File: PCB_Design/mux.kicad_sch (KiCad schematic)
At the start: 8 parts, among them U26 SN74HC595, U27 SN74HC595, U28 ADG1406BRUZ-REEL7, U29 ADG1406BRUZ-REEL7, U30 ADG1406BRUZ-REEL7, U31 ADG1406BRUZ-REEL7

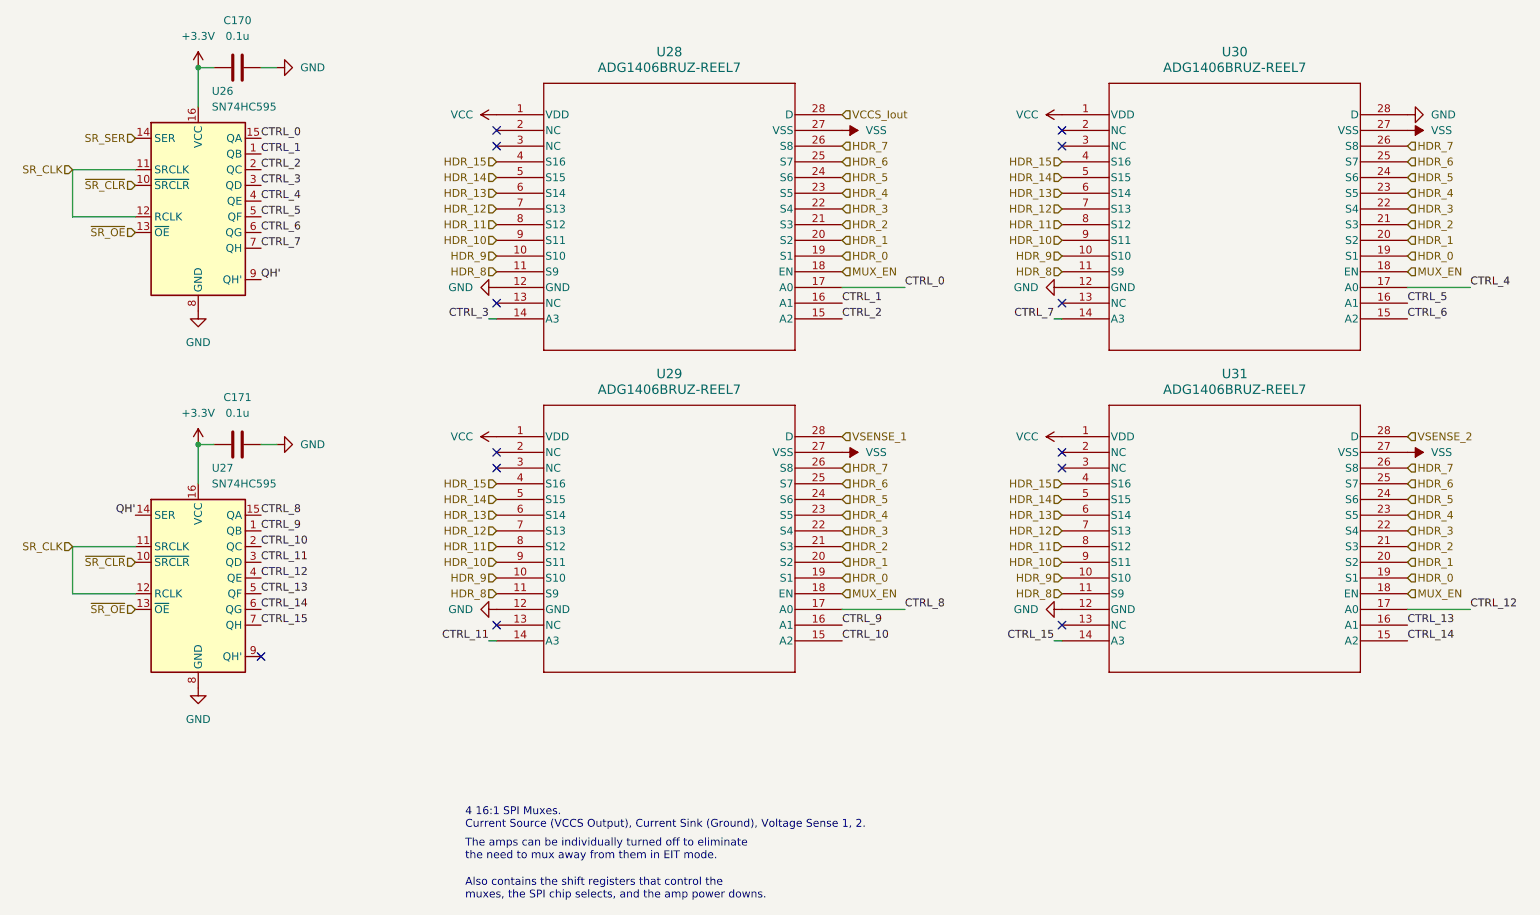
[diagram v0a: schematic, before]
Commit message: KiCAD file update, completed PCB
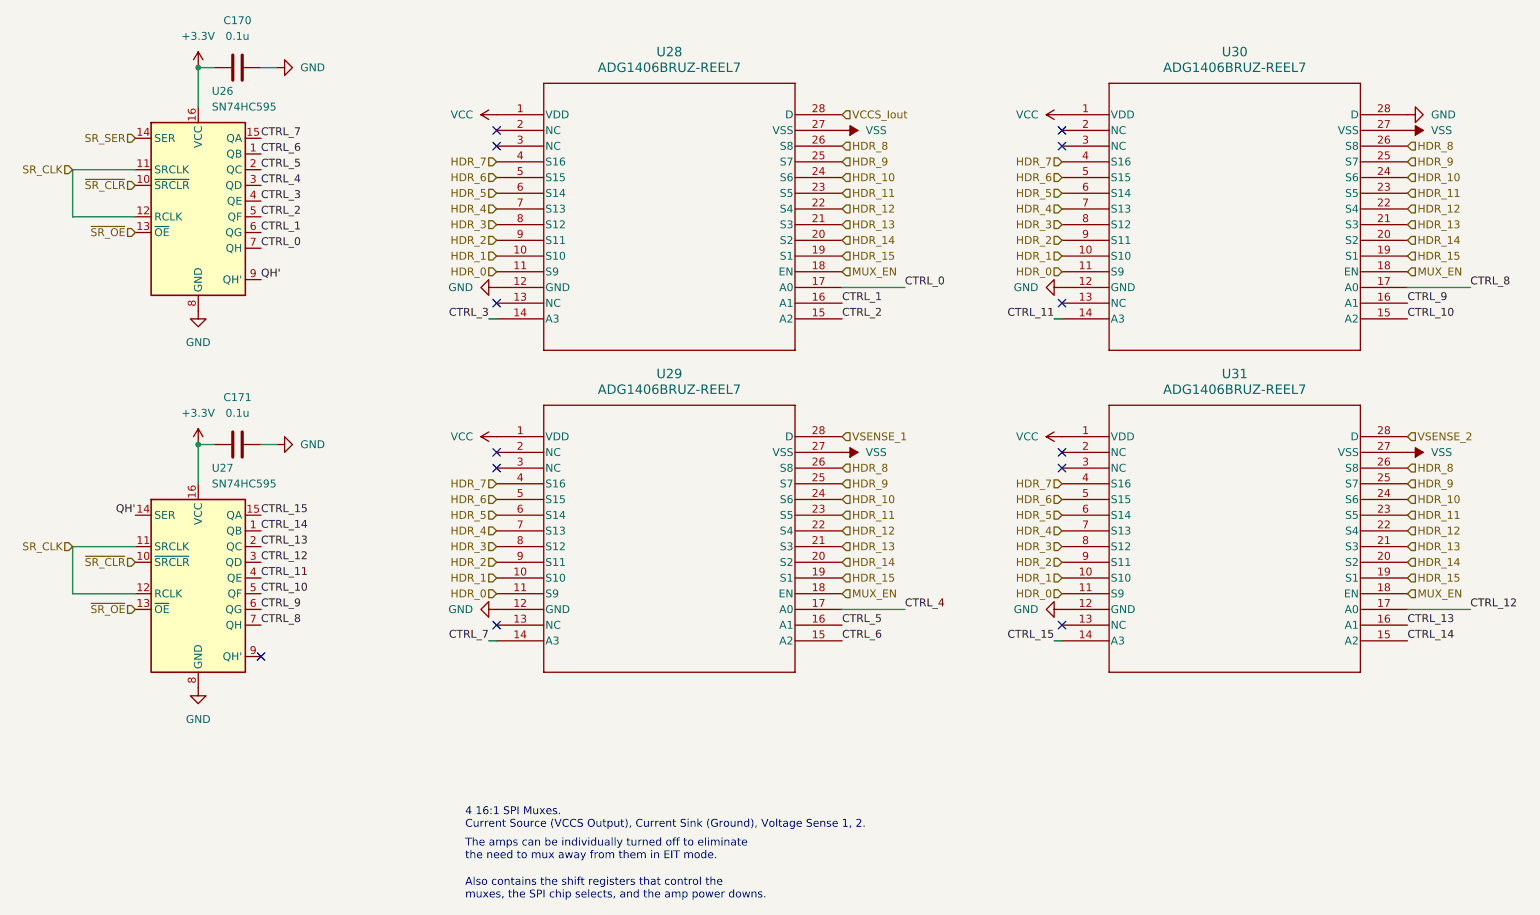
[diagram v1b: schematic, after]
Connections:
- net CTRL_0: now also U26.7 (QH); no longer U26.15 (QA)
- net CTRL_1: now also U26.6 (QG); no longer U26.1 (QB)
- net CTRL_10: now also U27.5 (QF), U30.15 (A2); no longer U27.2 (QC), U29.15 (A2)
- net CTRL_11: now also U27.4 (QE), U30.14 (A3); no longer U27.3 (QD), U29.14 (A3)
- net CTRL_12: now also U27.3 (QD); no longer U27.4 (QE)
- net CTRL_13: now also U27.2 (QC); no longer U27.5 (QF)
- net CTRL_14: now also U27.1 (QB); no longer U27.6 (QG)
- net CTRL_15: now also U27.15 (QA); no longer U27.7 (QH)
- net CTRL_2: now also U26.5 (QF); no longer U26.2 (QC)
- net CTRL_3: now also U26.4 (QE); no longer U26.3 (QD)
- net CTRL_4: now also U26.3 (QD), U29.17 (A0); no longer U26.4 (QE), U30.17 (A0)
- net CTRL_5: now also U26.2 (QC), U29.16 (A1); no longer U26.5 (QF), U30.16 (A1)
- net CTRL_6: now also U26.1 (QB), U29.15 (A2); no longer U26.6 (QG), U30.15 (A2)
- net CTRL_7: now also U26.15 (QA), U29.14 (A3); no longer U26.7 (QH), U30.14 (A3)
- net CTRL_8: now also U27.7 (QH), U30.17 (A0); no longer U27.15 (QA), U29.17 (A0)
- net CTRL_9: now also U27.6 (QG), U30.16 (A1); no longer U27.1 (QB), U29.16 (A1)
- net HDR_0: now also U28.11 (S9), U29.11 (S9), U30.11 (S9), U31.11 (S9); no longer U28.19 (S1), U29.19 (S1), U30.19 (S1), U31.19 (S1)
- net HDR_1: now also U28.10 (S10), U29.10 (S10), U30.10 (S10), U31.10 (S10); no longer U28.20 (S2), U29.20 (S2), U30.20 (S2), U31.20 (S2)
- net HDR_10: now also U28.24 (S6), U29.24 (S6), U30.24 (S6), U31.24 (S6); no longer U28.9 (S11), U29.9 (S11), U30.9 (S11), U31.9 (S11)
- net HDR_11: now also U28.23 (S5), U29.23 (S5), U30.23 (S5), U31.23 (S5); no longer U28.8 (S12), U29.8 (S12), U30.8 (S12), U31.8 (S12)
- net HDR_12: now also U28.22 (S4), U29.22 (S4), U30.22 (S4), U31.22 (S4); no longer U28.7 (S13), U29.7 (S13), U30.7 (S13), U31.7 (S13)
- net HDR_13: now also U28.21 (S3), U29.21 (S3), U30.21 (S3), U31.21 (S3); no longer U28.6 (S14), U29.6 (S14), U30.6 (S14), U31.6 (S14)
- net HDR_14: now also U28.20 (S2), U29.20 (S2), U30.20 (S2), U31.20 (S2); no longer U28.5 (S15), U29.5 (S15), U30.5 (S15), U31.5 (S15)
- net HDR_15: now also U28.19 (S1), U29.19 (S1), U30.19 (S1), U31.19 (S1); no longer U28.4 (S16), U29.4 (S16), U30.4 (S16), U31.4 (S16)
- net HDR_2: now also U28.9 (S11), U29.9 (S11), U30.9 (S11), U31.9 (S11); no longer U28.21 (S3), U29.21 (S3), U30.21 (S3), U31.21 (S3)
- net HDR_3: now also U28.8 (S12), U29.8 (S12), U30.8 (S12), U31.8 (S12); no longer U28.22 (S4), U29.22 (S4), U30.22 (S4), U31.22 (S4)
- net HDR_4: now also U28.7 (S13), U29.7 (S13), U30.7 (S13), U31.7 (S13); no longer U28.23 (S5), U29.23 (S5), U30.23 (S5), U31.23 (S5)
- net HDR_5: now also U28.6 (S14), U29.6 (S14), U30.6 (S14), U31.6 (S14); no longer U28.24 (S6), U29.24 (S6), U30.24 (S6), U31.24 (S6)
- net HDR_6: now also U28.5 (S15), U29.5 (S15), U30.5 (S15), U31.5 (S15); no longer U28.25 (S7), U29.25 (S7), U30.25 (S7), U31.25 (S7)
- net HDR_7: now also U28.4 (S16), U29.4 (S16), U30.4 (S16), U31.4 (S16); no longer U28.26 (S8), U29.26 (S8), U30.26 (S8), U31.26 (S8)
- net HDR_8: now also U28.26 (S8), U29.26 (S8), U30.26 (S8), U31.26 (S8); no longer U28.11 (S9), U29.11 (S9), U30.11 (S9), U31.11 (S9)
- net HDR_9: now also U28.25 (S7), U29.25 (S7), U30.25 (S7), U31.25 (S7); no longer U28.10 (S10), U29.10 (S10), U30.10 (S10), U31.10 (S10)
